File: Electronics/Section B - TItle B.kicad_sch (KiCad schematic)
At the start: 28 parts, among them J5 JST_SHBM04B-SRSS-TB, J6 Conn_02x07_Odd_Even, J7 THD-20-R, J9 Micro_SD_Card_Det, SW1 Right angle Tact button, U3 74LVC1G07SE-7, U6 RT9742GGJ5

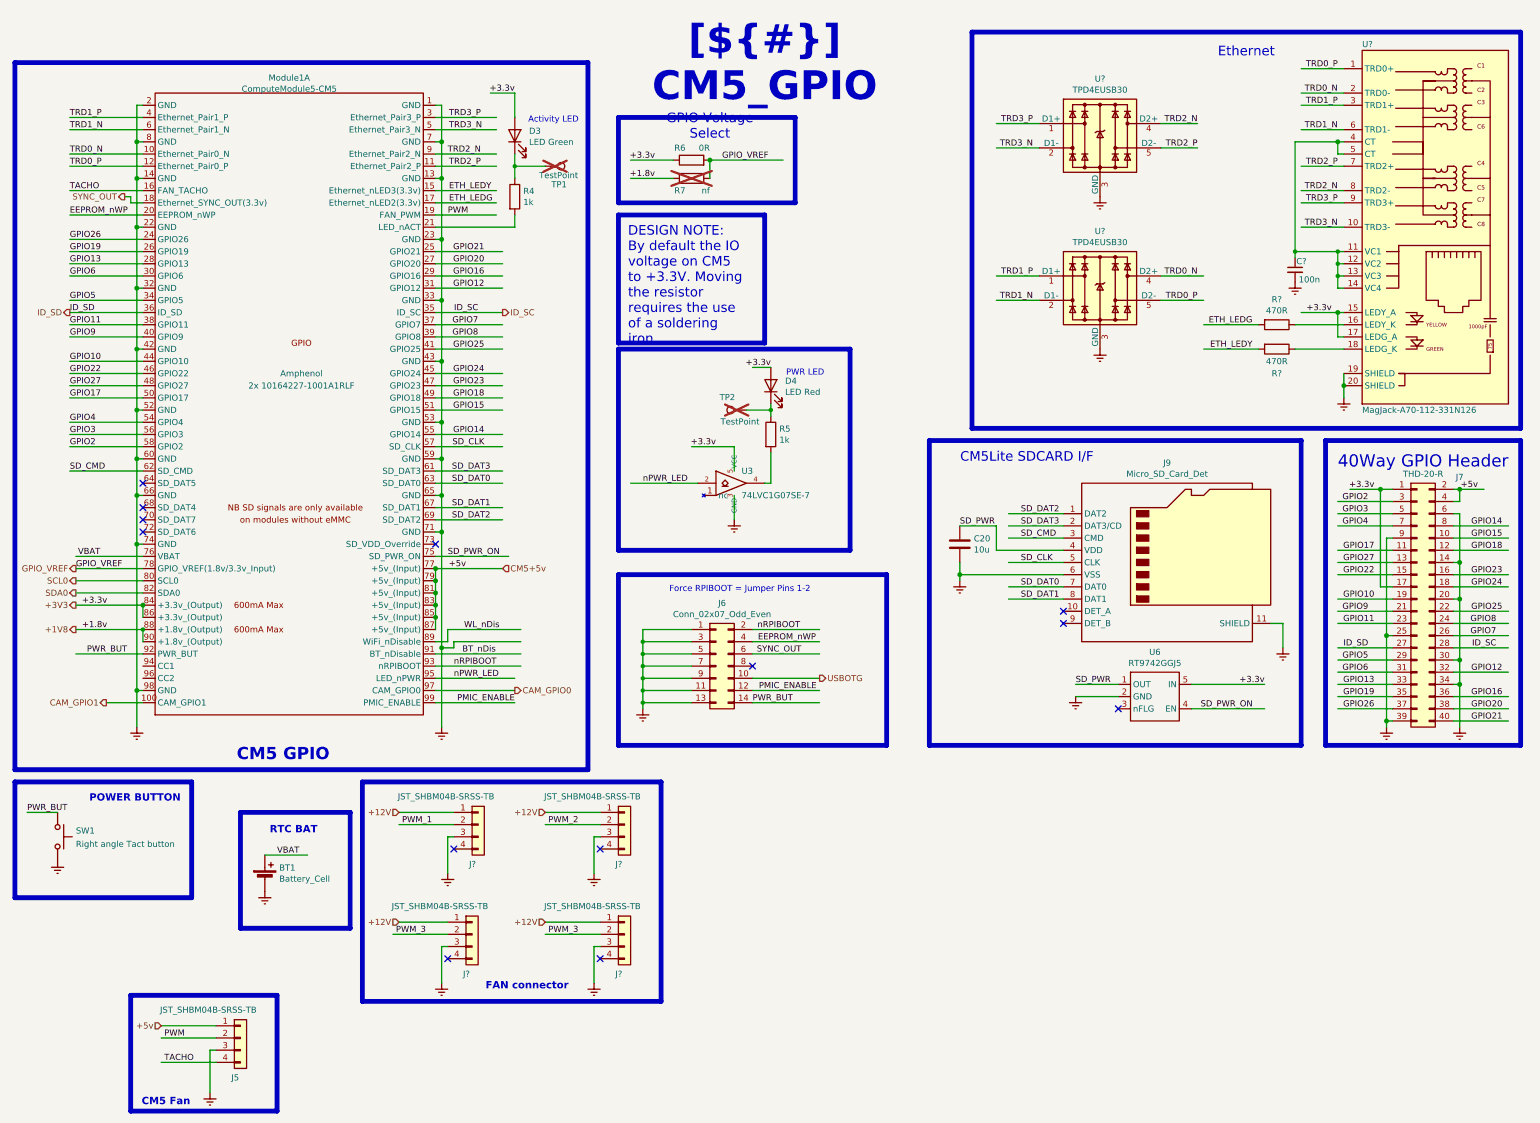
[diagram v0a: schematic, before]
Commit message: RP2040 Added, Files Structure Changed
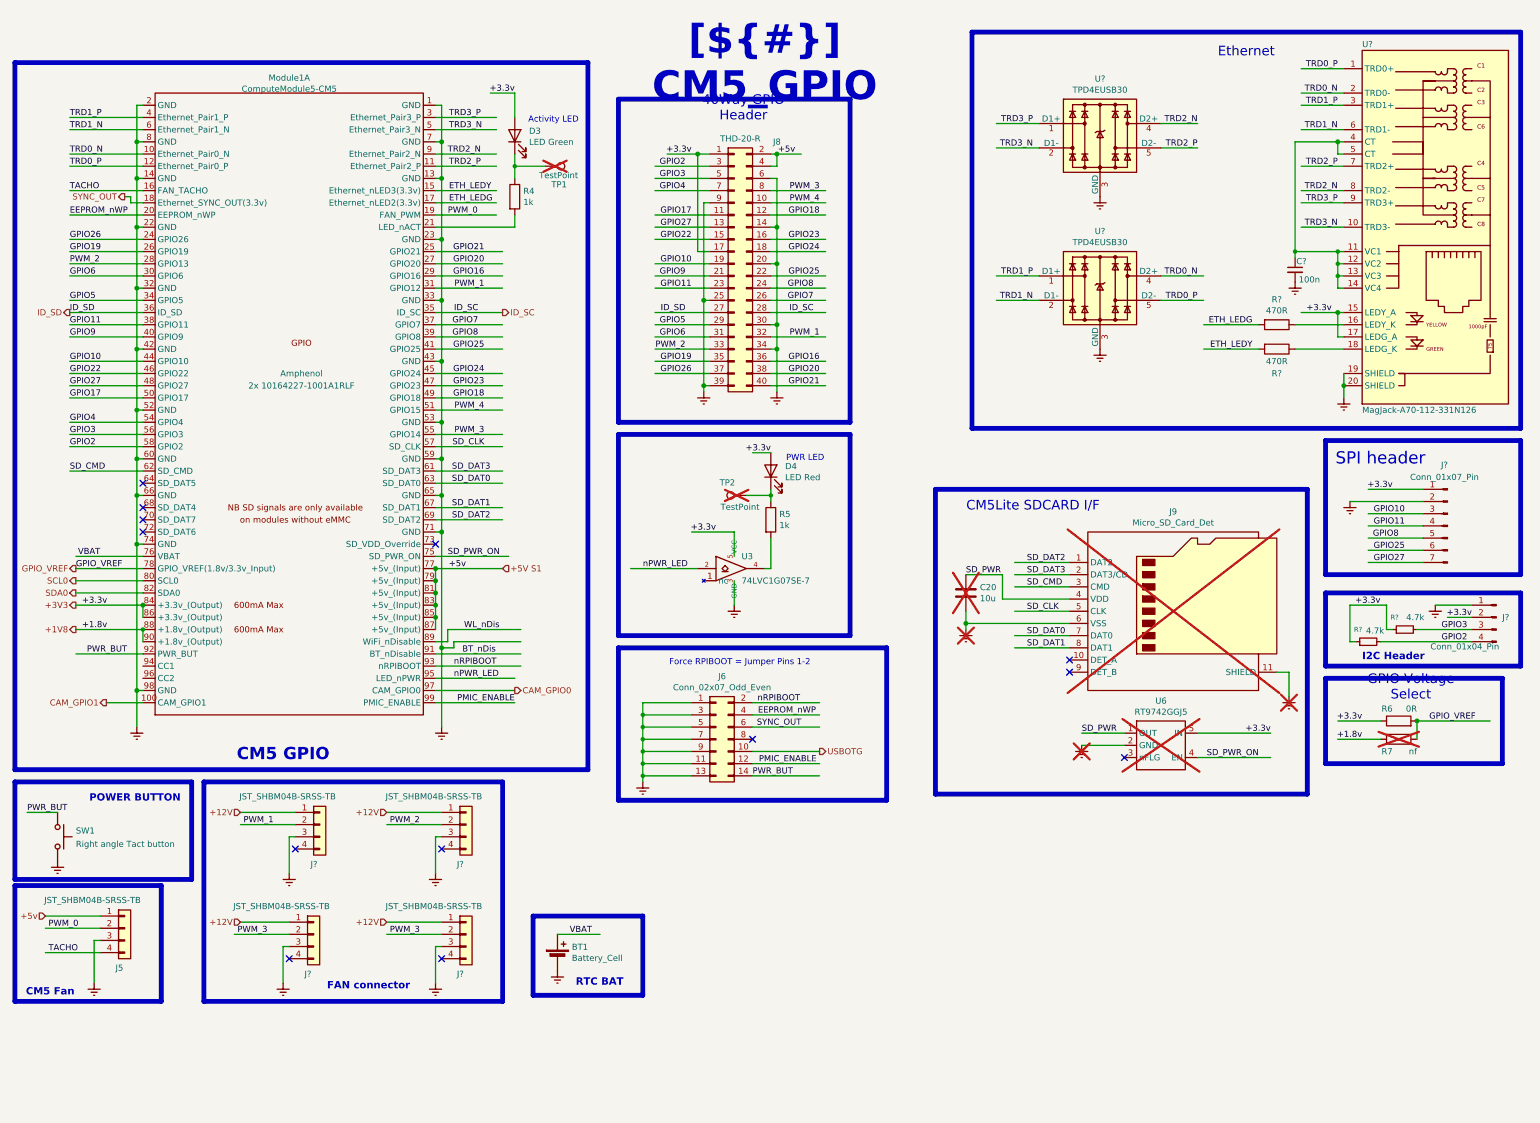
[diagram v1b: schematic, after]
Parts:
- added J?: Conn_01x07_Pin, symbol Connector:Conn_01x07_Pin
- added J?: Conn_01x04_Pin, symbol Connector:Conn_01x04_Pin
- added R? (x2): 4.7k, symbol Device:R_Small
- C20, J9, U6: now not fitted; now left out of the parts list
- renumbered J7 to J8
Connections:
- net GPIO12 is gone; now on net PWM_1: J8.32 (Pin_32), Module1.31 (GPIO12)
- net GPIO13 is gone; now on net PWM_2: J8.33 (Pin_33), Module1.28 (GPIO13)
- net GPIO14 is gone; now on net PWM_3: J8.8 (Pin_8), Module1.55 (GPIO14)
- net +3V3: now also J?.1 (Pin_1), J?.2 (Pin_2), R?.1, R?.1
- net GPIO10: now also J?.3 (Pin_3)
- net GPIO11: now also J?.4 (Pin_4)
- net GPIO2: now also J?.4 (Pin_4), R?.2
- net GPIO25: now also J?.6 (Pin_6)
- net GPIO27: now also J?.7 (Pin_7)
- net GPIO3: now also J?.3 (Pin_3), R?.2
- net GPIO8: now also J?.5 (Pin_5)
- net +5v renamed +5V S1
- net GPIO15 renamed PWM_4
- net PWM renamed PWM_0
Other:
- note added: "I2C Header"
- moved on the sheet: BT1, D4, J5, J6, J8, J?, R5, R6, R7, TP2, U3

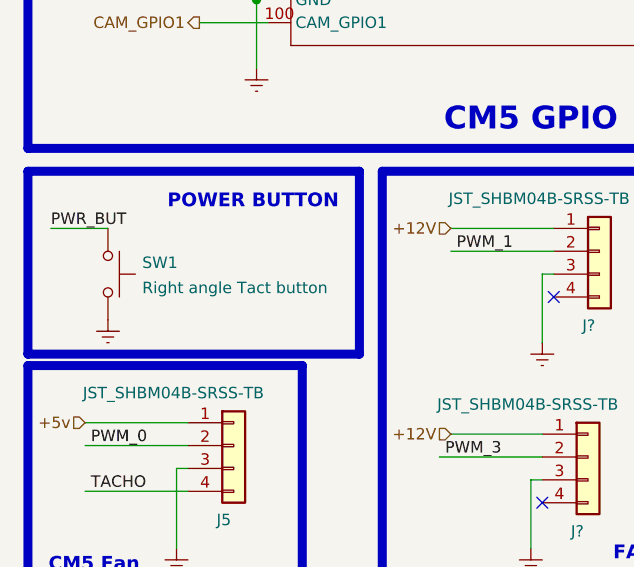
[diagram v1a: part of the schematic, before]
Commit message: Rp2040 Power Sequence finished and general cleaning
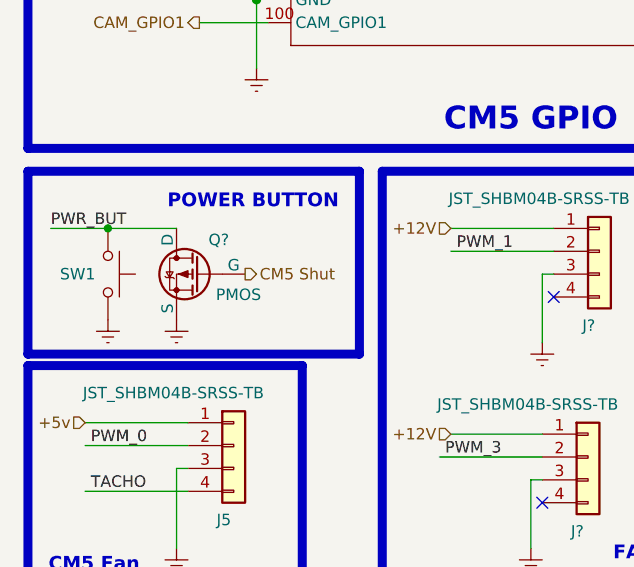
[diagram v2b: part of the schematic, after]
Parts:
- added Q?: PMOS, symbol Simulation_SPICE:PMOS
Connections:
- net PWR_BUT: now also Q?.1 (D)
- new net CM5 Shut: Q?.2 (G)
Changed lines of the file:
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@@
 	)
 	(junction
+		(at 22.86 176.53)
+		(diameter 0)
+		(color 0 0 0 0)
+	)
+	(junction
 		(at 290.83 87.63)
 		(diameter 1.016)
@@
 	(wire
 		(pts
+			(xy 22.86 176.53) (xy 30.48 176.53)
+		)
+		(stroke
+			(width 0)
+			(type default)
+		)
+	)
+	(wire
+		(pts
 			(xy 147.32 52.07) (xy 158.75 52.07)
 		)
@@
 		)
 	)
+	(hierarchical_label "CM5 Shut"
+		(shape output)
+		(at 38.1 181.61 0)
+		(effects
+			(font
+				(size 1.27 1.27)
+			)
+			(justify left)
+		)
+	)
 	(hierarchical_label "ID_SD"
 		(shape output)
@@
 		(dnp no)
 		(property "Reference" "SW1"
-			(at 26.67 180.3399 90)
+			(at 17.526 181.61 90)
 			(effects
 				(font
@@
 				)
 				(justify left)
+				(hide yes)
 			)
 		)
@@
 	)
 	(symbol
+		(lib_id "Simulation_SPICE:PMOS")
+		(at 33.02 181.61 0)
+		(mirror y)
+		(unit 1)
+		(exclude_from_sim no)
+		(in_bom yes)
+		(on_board yes)
+		(dnp no)
+		(property "Reference" "Q?"
+			(at 36.322 177.8 0)
+			(effects
+				(font
+					(size 1.27 1.27)
+				)
+				(justify left)
+			)
+		)
+		(property "Value" "PMOS"
+			(at 39.878 183.896 0)
+			(effects
+				(font
+					(size 1.27 1.27)
+				)
+				(justify left)
+			)
+		)
+		(property "Footprint" ""
+			(at 27.94 179.07 0)
+			(effects
+				(font
+					(size 1.27 1.27)
+				)
+				(hide yes)
+			)
+		)
+		(property "Datasheet" "https://ngspice.sourceforge.io/docs/ngspice-html-manual/manual.xhtml#cha_MOSFETs"
+			(at 33.02 194.31 0)
+			(effects
+				(font
+					(size 1.27 1.27)
+				)
+				(hide yes)
+			)
+		)
+		(property "Description" "P-MOSFET transistor, drain/source/gate"
+			(at 33.02 181.61 0)
+			(effects
+				(font
+					(size 1.27 1.27)
+				)
+				(hide yes)
+			)
+		)
+		(property "Sim.Device" "PMOS"
+			(at 33.02 198.755 0)
+			(effects
+				(font
+					(size 1.27 1.27)
+				)
+				(hide yes)
+			)
+		)
+		(property "Sim.Type" "VDMOS"
+			(at 33.02 200.66 0)
+			(effects
+				(font
+					(size 1.27 1.27)
+				)
+				(hide yes)
+			)
+		)
+		(property "Sim.Pins" "1=D 2=G 3=S"
+			(at 33.02 196.85 0)
+			(effects
+				(font
+					(size 1.27 1.27)
+				)
+				(hide yes)
+			)
+		)
+		(pin "3"
+		)
+		(pin "1"
+		)
+		(pin "2"
+		)
+		(instances
+			(project "CM5 Nas"
+				(path "/0650c7a8-acba-429c-9f8e-eec0baf0bc1c/fede4c36-00cc-4d3d-b71c-5243ba232202/e6015f1e-cbce-46f4-85e1-3d5463a17dc1"
+					(reference "Q?")
+					(unit 1)
+				)
+			)
+		)
+	)
+	(symbol
 		(lib_id "CM5IO:ComputeModule5-CM5")
 		(at 73.66 85.09 0)
@@
 					(unit 1)
 				)
+			)
+		)
+	)
+	(symbol
+		(lib_id "power:Earth")
+		(at 30.48 186.69 0)
+		(unit 1)
+		(exclude_from_sim no)
+		(in_bom yes)
+		(on_board yes)
+		(dnp no)
+		(property "Reference" "#PWR0173"
+			(at 30.48 193.04 0)
+			(effects
+				(font
+					(size 1.27 1.27)
+				)
+				(hide yes)
+			)
+		)
+		(property "Value" "~"
+			(at 30.48 190.5 0)
+			(effects
+				(font
+					(size 1.27 1.27)
+				)
+			)
+		)
+		(property "Footprint" ""
+			(at 30.48 186.69 0)
+			(effects
+				(font
+					(size 1.27 1.27)
+				)
+				(hide yes)
+			)
+		)
+		(property "Datasheet" "~"
+			(at 30.48 186.69 0)
+			(effects
+				(font
+					(size 1.27 1.27)
+				)
+				(hide yes)
+			)
+		)
+		(property "Description" "Power symbol creates a global label with name \"Earth\""
+			(at 30.48 186.69 0)
+			(effects
+				(font
+					(size 1.27 1.27)
+				)
+				(hide yes)
+			)
+		)
+		(pin "1"
+		)
+		(instances
+			(project "CM5 Nas"
+				(path "/0650c7a8-acba-429c-9f8e-eec0baf0bc1c/fede4c36-00cc-4d3d-b71c-5243ba232202/e6015f1e-cbce-46f4-85e1-3d5463a17dc1"
+					(reference "#PWR0173")
+					(unit 1)
+				)

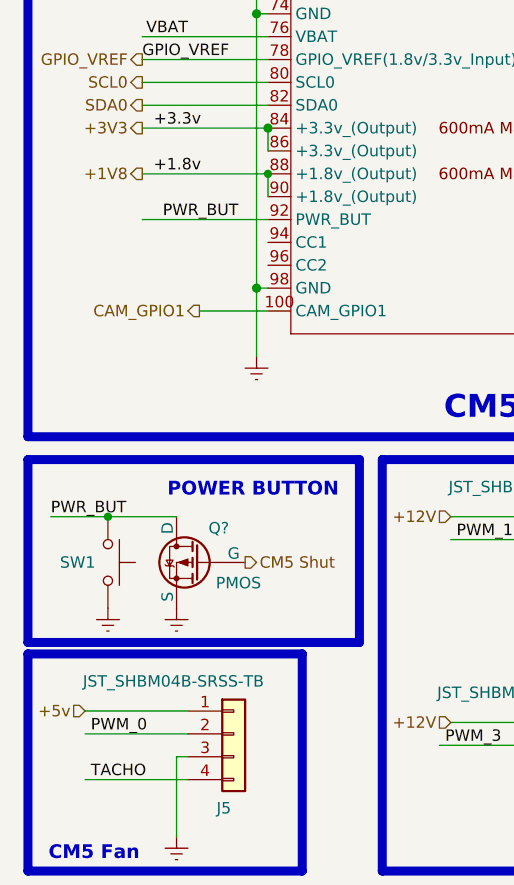
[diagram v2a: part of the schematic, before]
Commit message: Starting the Sheet connections
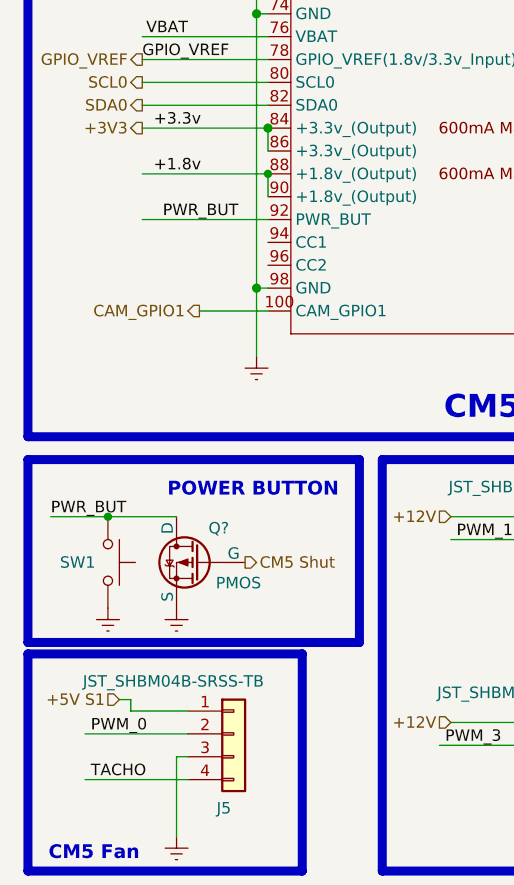
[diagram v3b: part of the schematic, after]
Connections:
- net +1V8 renamed +1.8v
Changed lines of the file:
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@@
 	(wire
 		(pts
-			(xy 20.32 198.12) (xy 31.75 198.12)
+			(xy 24.13 196.85) (xy 25.4 196.85)
 		)
 		(stroke
@@
 	(wire
 		(pts
+			(xy 25.4 196.85) (xy 25.4 198.12)
+		)
+		(stroke
+			(width 0)
+			(type solid)
+		)
+	)
+	(wire
+		(pts
 			(xy 295.91 109.22) (xy 307.34 109.22)
 		)
@@
 	(wire
 		(pts
+			(xy 25.4 198.12) (xy 31.75 198.12)
+		)
+		(stroke
+			(width 0)
+			(type solid)
+		)
+	)
+	(wire
+		(pts
 			(xy 280.67 36.83) (xy 289.56 36.83)
 		)
@@
 		)
 	)
-	(hierarchical_label "+1V8"
-		(shape output)
-		(at 26.67 138.43 180)
-		(effects
-			(font
-				(size 1.27 1.27)
-			)
-			(justify right)
-		)
-	)
 	(hierarchical_label "CM5 Shut"
 		(shape output)
@@
 		)
 	)
-	(hierarchical_label "+5v"
+	(hierarchical_label "+5V S1"
 		(shape input)
-		(at 20.32 198.12 180)
+		(at 24.13 196.85 180)
 		(effects
 			(font

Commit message: Footprints Selected
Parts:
- removed C?: 100n, symbol Device:C_Small
- removed R?: 470R, Resistor_SMD:R_0402_1005Metric, symbol Device:R
- removed U?: MagJack-A70-112-331N126, CM5IO:TRJG0926HENL, symbol CM5IO:MagJack-A70-112-331N126
- added J12: RJ45_RB1-125B8G1A, Connector_RJ:RJ45_UDE_RB1-125B8G1A, symbol Connector:RJ45_RB1-125B8G1A
- added R6: 1K, Resistor_SMD:R_0603_1608Metric, symbol Device:R
- BT1: footprint CM5IO:BatteryHolder_Keystone_3034_1x20mm -> Battery:BatteryHolder_Keystone_3034_1x20mm
- J13: renamed from J?; value Conn_01x07_Pin -> Conn_01x07; footprint (none) -> Connector_JST:JST_GH_SM07B-GHS-TB_1x07-1MP_P1.25mm_Horizontal; symbol Connector:Conn_01x07_Pin -> Connector:Conn_01x07_Socket
- J14: renamed from J?; value Conn_01x04_Pin -> Conn_01x04; footprint (none) -> PRT-14417:SPARKFUN_PRT-14417; symbol Connector:Conn_01x04_Pin -> Connector:Conn_01x04_Socket
- Module1: footprint CM5IO:Raspberry-Pi-5-Compute-Module -> cm5:Raspberry-Pi-5-Compute-Module
- Q1: renamed from Q?; footprint (none) -> BSS84AKW115:BSS84AKW115
- R10, R5: renamed from R?; footprint (none) -> Resistor_SMD:R_0603_1608Metric
- R3: renamed from R4; footprint Resistor_SMD:R_0402_1005Metric -> Resistor_SMD:R_0603_1608Metric
- R4: renamed from R5; footprint Resistor_SMD:R_0402_1005Metric -> Resistor_SMD:R_0603_1608Metric
- R9: renamed from R?; value 470R -> 1K; footprint Resistor_SMD:R_0402_1005Metric -> Resistor_SMD:R_0603_1608Metric
- TP1, TP2: footprint TestPoint:TestPoint_Pad_2.0x2.0mm -> TestPoint:TestPoint_Pad_1.0x1.0mm
- gave numbers to parts that had none: 6
- renumbered C20 to C3, D3 to D1, D4 to D2, J8 to J10, J9 to J11, J5 to J4, J6 to J9, R6 to R7, R7 to R8, U3 to U2, U6 to U5
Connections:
- net +3V3: now also J12.L1, J12.L3
- net ETH_LEDG: now also R6.1
- net ETH_LEDY: now also R9.1; no longer R9.2
- net TRD0_N: now also J12.R3 (TD1-)
- net TRD0_P: now also J12.R2 (TD1+)
- net TRD1_N: now also J12.R5 (TD2-)
- net TRD1_P: now also J12.R4 (TD2+)
- net TRD2_N: now also J12.R7 (TD3-)
- net TRD2_P: now also J12.R6 (TD3+)
- net TRD3_N: now also J12.R9 (TD4-)
- net TRD3_P: now also J12.R8 (TD4+)
- net +1.8v renamed +1V8
- new net: J12.L4, R6.2
- new net: J12.L2, R9.2
- new net: J12.R10 (GND), J12.SH
- new net +3V3A: J12.R1 (CT)
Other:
- moved on the sheet: R9

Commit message: Footprints selected, Hiracicle connections created, Pcb next
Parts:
- J7: renamed from J11; footprint CM5IO:SDCARD_MOLEX_503398-1892 -> DM3AT-SF-PEJM5:DM3ATSFPEJM5
- R5: renamed from R3; value 1k -> 1K
- R7: renamed from R10; value 4.7k -> 4K7
- R8: renamed from R5; value 4.7k -> 4K7
- renumbered J6 to J10, J7 to J11, J4 to J12, J5 to J13, J8 to J14, J10 to J4, J12 to J5, J13 to J6, J14 to J8, R8 to R10, R9 to R3, R6 to R4, R4 to R6, R7 to R9, U3 to U2, U4 to U3, U2 to U4
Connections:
- net +3V3A is gone; now on net +3V3: J5.R1 (CT)
- net CM5 Shut: now also Module1.54 (GPIO4)
- net ETH_LEDG: now also R3.1; no longer R4.1
- net ETH_LEDY: now also R4.1; no longer R3.1
- net GPIO10: no longer J4.19 (Pin_19)
- net GPIO11: no longer J4.23 (Pin_23)
- net GPIO2: no longer J4.3 (Pin_3)
- net GPIO25: no longer J4.22 (Pin_22)
- net GPIO27: no longer J4.13 (Pin_13)
- net GPIO3: no longer J4.5 (Pin_5)
- net GPIO8: no longer J4.24 (Pin_24)
- net PWM_1: no longer J4.32 (Pin_32)
- net PWM_2: no longer J4.33 (Pin_33)
- net PWM_3: no longer J4.8 (Pin_8)
- net PWM_4: no longer J4.10 (Pin_10)
- net gnd: now reaches U4.3 (GND)
- net gnd: now also BT1.2 (-), C3.2, J10.3 (Pin_3), J11.3 (Pin_3), J12.3 (Pin_3), J13.3 (Pin_3), J14.3 (Pin_3), J4.14 (Pin_14), J4.20 (Pin_20), J4.25 (Pin_25), J4.30 (Pin_30), J4.34 (Pin_34), J4.39 (Pin_39), J4.6 (Pin_6), J4.9 (Pin_9), J5.R10 (GND), J5.SH, J6.2 (Pin_2), J7.11 (SHIELD), J7.6 (VSS), J8.1 (Pin_1), J9.1 (Pin_1), J9.11 (Pin_11), J9.13 (Pin_13), J9.3 (Pin_3), J9.5 (Pin_5), J9.7 (Pin_7), J9.9 (Pin_9), Module1.1 (GND), Module1.13 (GND), Module1.14 (GND), Module1.2 (GND), Module1.22 (GND), Module1.23 (GND), Module1.32 (GND), Module1.33 (GND), Module1.42 (GND), Module1.43 (GND), Module1.52 (GND), Module1.53 (GND), Module1.59 (GND), Module1.60 (GND), Module1.65 (GND), Module1.66 (GND), Module1.7 (GND), Module1.71 (GND), Module1.74 (GND), Module1.8 (GND), Module1.98 (GND), Q1.3 (S), SW1.2, U2.3 (GND), U2.8 (GND), U3.3 (GND), U3.8 (GND), U5.2 (GND)
- net GPIO4: no longer names the net of J4.7 (Pin_7)
- net GPIO4: no longer Module1.54 (GPIO4)
- no-connect marks 13 -> 25
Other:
- moved on the sheet: J5, R3, R4
